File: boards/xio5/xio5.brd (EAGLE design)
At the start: 170 x 170 mm, 79 parts

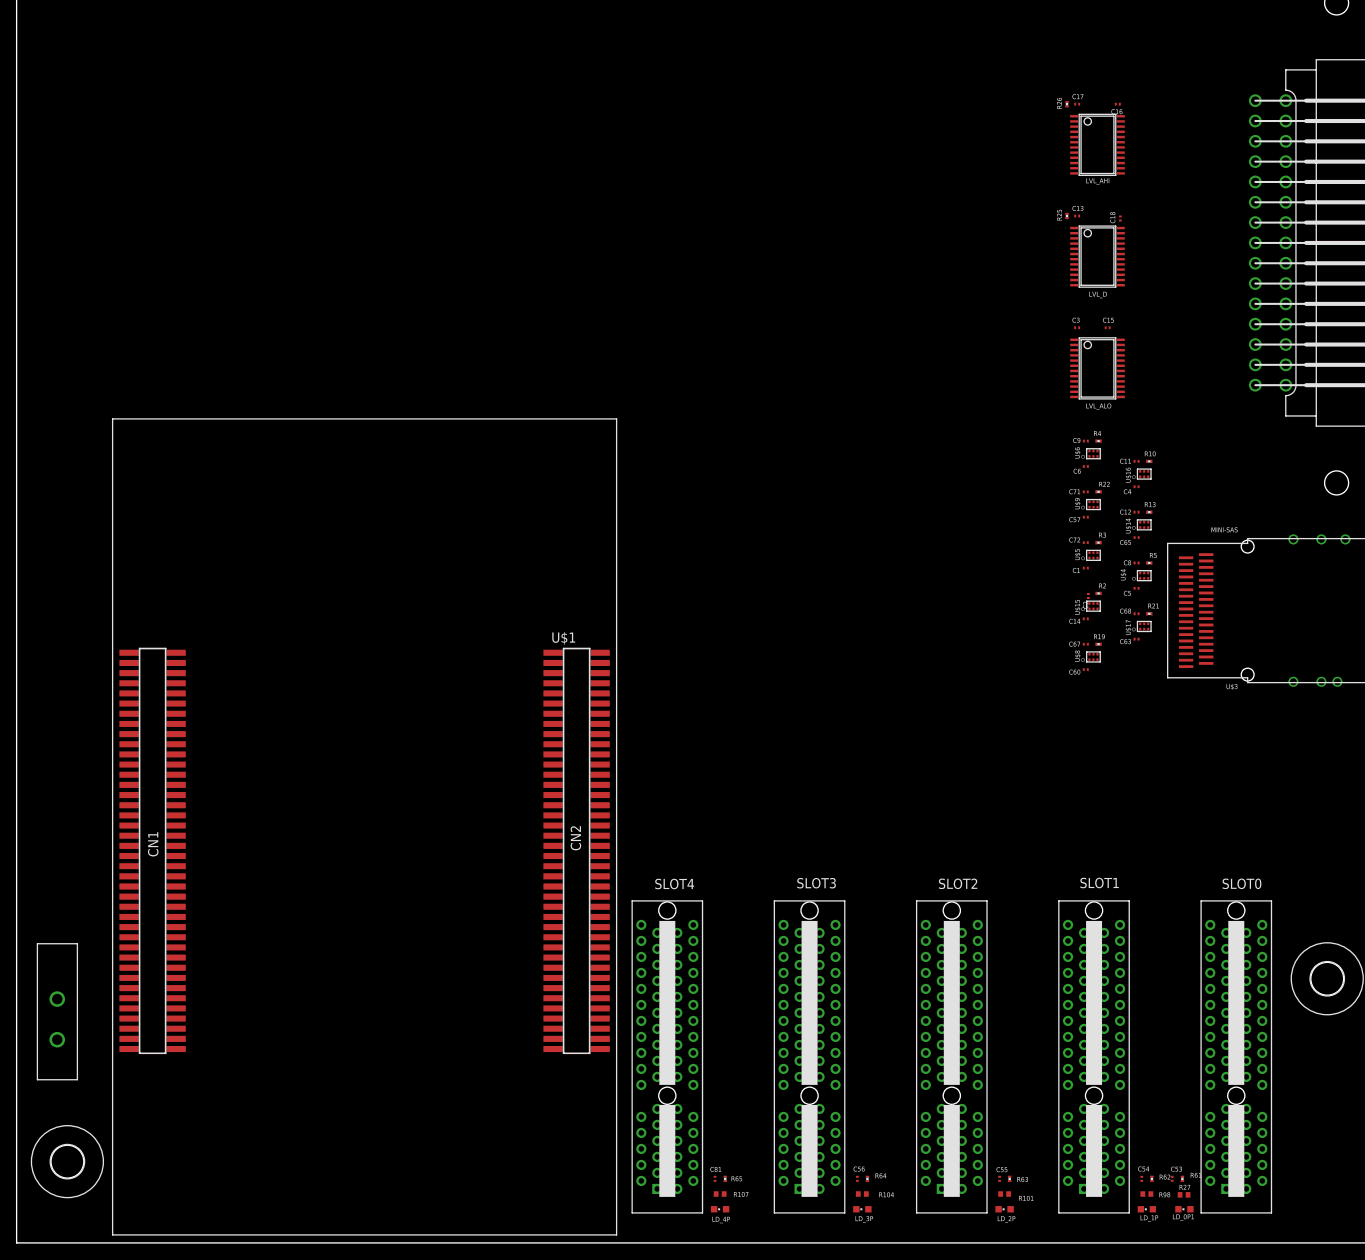
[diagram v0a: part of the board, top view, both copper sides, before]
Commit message: Start adding busses
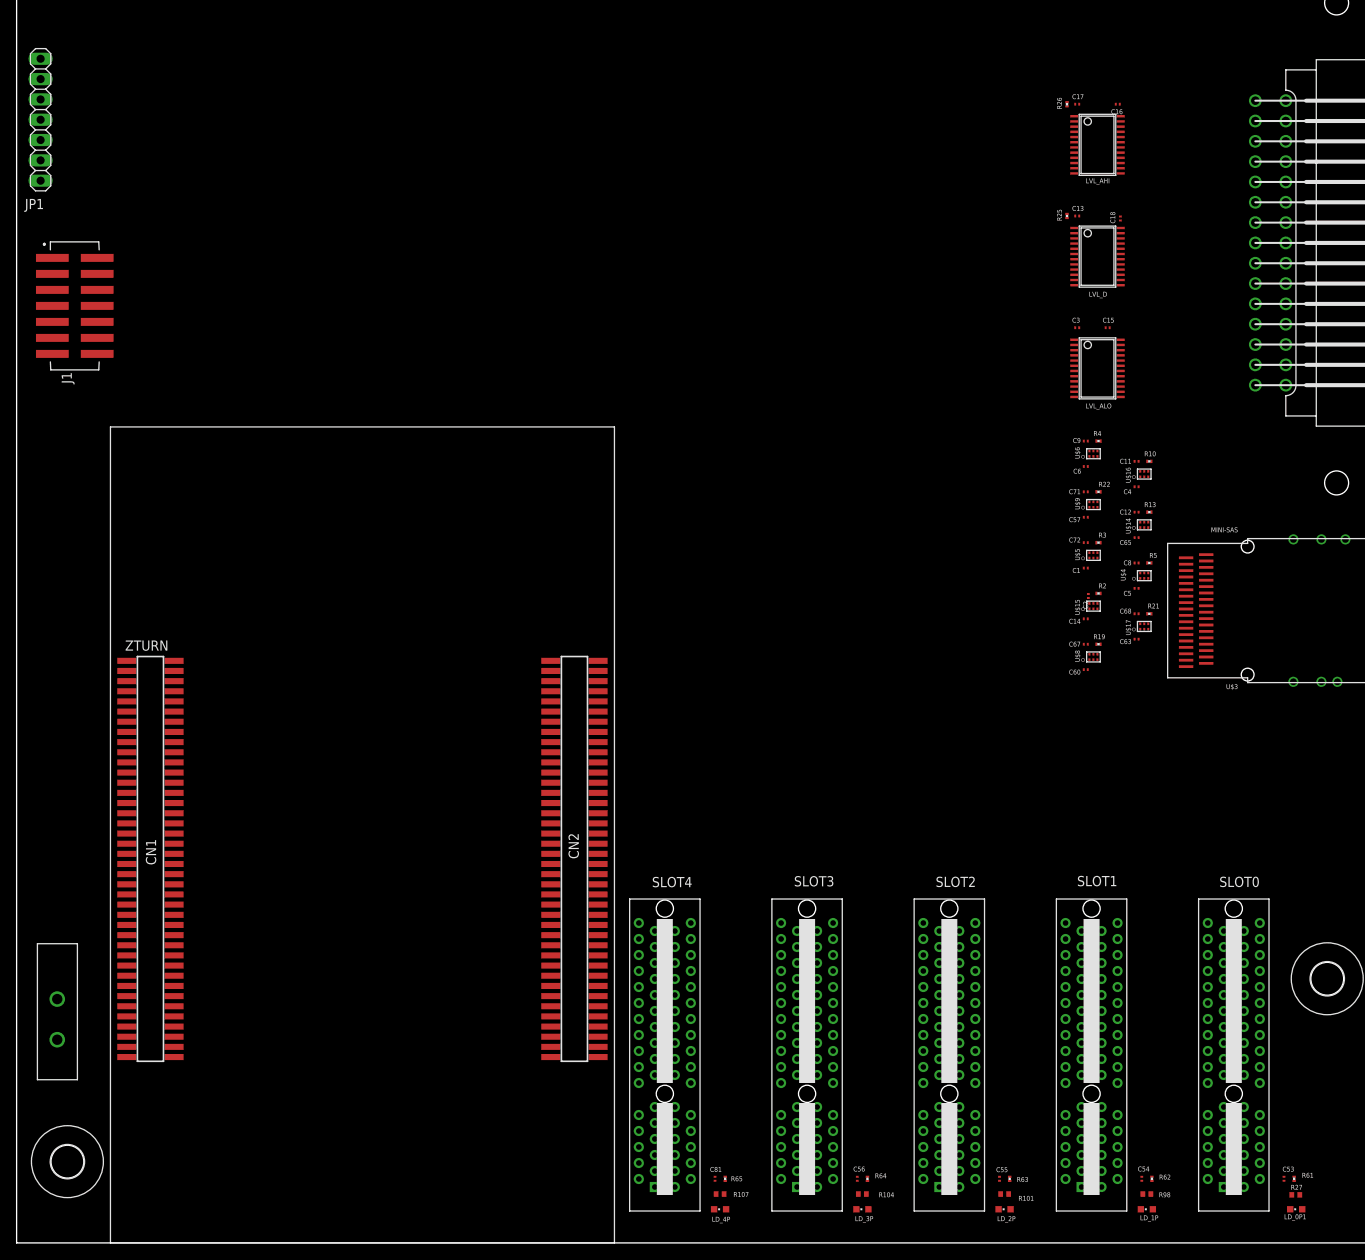
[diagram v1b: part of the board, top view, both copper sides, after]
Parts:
- removed U$1: ZTURN, pbxl:ZTURN
- added J1: 98424-G52-14ALF, samacsys:98424G5214ALF
- added JP1: (no value), pinhead:1X07
- added ZTURN: ZTURN, pbxl:ZTURN
- moved C53 14.0 mm to (158.4, 8.02)
- moved LD_0P1 14.0 mm to (159.9, 4.21)
- moved R27 14.0 mm to (159.9, 6.01)
- moved R61 14.0 mm to (159.7, 8.02)
- moved SLOT0 0.39 mm to (152.4, 19.1)
- moved SLOT1 0.39 mm to (134.6, 19.1)
- moved SLOT2 0.39 mm to (116.8, 19.1)
- moved SLOT3 0.39 mm to (99.1, 19.1)
- moved SLOT4 0.39 mm to (81.3, 19.1)
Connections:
- new net !SRST!: J1.B7, JP1.6, ZTURN.CN1_14
- new net TCK: J1.B3, JP1.3, ZTURN.CN1_6
- new net TDI: J1.B5, JP1.5, ZTURN.CN1_10
- new net TDO: J1.B4, JP1.4, ZTURN.CN1_12
- new net TMS: J1.B2, JP1.2, ZTURN.CN1_8
- net +3V3: now also J1.B1, JP1.1, ZTURN.CN1_15, ZTURN.CN1_3, ZTURN.CN1_49, ZTURN.CN2_3, ZTURN.CN2_51
- net +5V: now also ZTURN.CN1_1, ZTURN.CN2_1
- net GND: now also J1.A1, J1.A2, J1.A3, J1.A4, J1.A5, J1.A6, J1.A7, JP1.7, ZTURN.CN1_2, ZTURN.CN1_24, ZTURN.CN1_25, ZTURN.CN1_34, ZTURN.CN1_35, ZTURN.CN1_4, ZTURN.CN1_44, ZTURN.CN1_54, ZTURN.CN1_67, ZTURN.CN1_68, ZTURN.CN2_2, ZTURN.CN2_20, ZTURN.CN2_21, ZTURN.CN2_30, ZTURN.CN2_31, ZTURN.CN2_4, ZTURN.CN2_40, ZTURN.CN2_41, ZTURN.CN2_50, ZTURN.CN2_60, ZTURN.CN2_61, ZTURN.CN2_70, ZTURN.CN2_71, ZTURN.CN2_80
- net LO_A0: now also ZTURN.CN2_59
- net LO_A1: now also ZTURN.CN2_57
- net LO_A10: now also ZTURN.CN2_35
- net LO_A11: now also ZTURN.CN2_33
- net LO_A12: now also ZTURN.CN2_29
- net LO_A13: now also ZTURN.CN2_27
- net LO_A14: now also ZTURN.CN2_25
- net LO_A15: now also ZTURN.CN2_23
- net LO_A2: now also ZTURN.CN2_55
- net LO_A3: now also ZTURN.CN2_53
- net LO_A4: now also ZTURN.CN2_49
- net LO_A5: now also ZTURN.CN2_47
- net LO_A6: now also ZTURN.CN2_45
- net LO_A7: now also ZTURN.CN2_43
- net LO_A8: now also ZTURN.CN2_39
- net LO_A9: now also ZTURN.CN2_37
- net LO_D0: now also ZTURN.CN2_79
- net LO_D1: now also ZTURN.CN2_77
- net LO_D2: now also ZTURN.CN2_75
- net LO_D3: now also ZTURN.CN2_73
- net LO_D4: now also ZTURN.CN2_69
- net LO_D5: now also ZTURN.CN2_67
- net LO_D6: now also ZTURN.CN2_65
- net LO_D7: now also ZTURN.CN2_63

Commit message: Reorganise slot signals (ZBUS) and add the internal slot expansion interface (XBUS)
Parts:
- moved LD_4P 72.4 mm to (160.3, 5.47)
- moved R107 72.4 mm to (160.3, 7.38)
- moved R65 72.4 mm to (161.0, 9.29)
- moved C81 72.4 mm to (159.7, 9.29)
- moved SLOT4 72.4 mm to (153.7, 20.3)
- moved C53 69.9 mm to (88.6, 9.29)
- moved LD_0P1 69.9 mm to (90.1, 5.47)
- moved R27 69.9 mm to (90.0, 7.28)
- moved SLOT0 69.9 mm to (82.5, 20.3)
- moved R61 69.9 mm to (89.8, 9.29)
- moved LD_3P 36.9 mm to (142.6, 5.47)
- moved R104 36.9 mm to (142.6, 7.38)
- moved C56 36.9 mm to (141.9, 9.29)
- moved R64 36.9 mm to (143.2, 9.29)
- moved SLOT3 36.9 mm to (135.9, 20.3)
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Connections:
- removed net !LO_CCTL!: SLOT0.A27, SLOT1.A27, SLOT2.A27, SLOT3.A27, SLOT4.A27
- removed net !LO_REF!: SLOT0.B15, SLOT1.B15, SLOT2.B15, SLOT3.B15, SLOT4.B15
- removed net HBUS0: SLOT0.B18, SLOT1.B18, SLOT2.B18, SLOT3.B18, SLOT4.B18
- removed net HBUS1: SLOT0.B19, SLOT1.B19, SLOT2.B19, SLOT3.B19, SLOT4.B19
- removed net HBUS10: SLOT0.B28, SLOT1.B28, SLOT2.B28, SLOT3.B28, SLOT4.B28
- removed net HBUS11: SLOT0.B29, SLOT1.B29, SLOT2.B29, SLOT3.B29, SLOT4.B29
- removed net HBUS12: SLOT0.B30, SLOT1.B30, SLOT2.B30, SLOT3.B30, SLOT4.B30
- removed net HBUS13: SLOT0.B31, SLOT1.B31, SLOT2.B31, SLOT3.B31, SLOT4.B31
- removed net HBUS2: SLOT0.B20, SLOT1.B20, SLOT2.B20, SLOT3.B20, SLOT4.B20
- removed net HBUS3: SLOT0.B21, SLOT1.B21, SLOT2.B21, SLOT3.B21, SLOT4.B21
- removed net HBUS4: SLOT0.B22, SLOT1.B22, SLOT2.B22, SLOT3.B22, SLOT4.B22
- removed net HBUS5: SLOT0.B23, SLOT1.B23, SLOT2.B23, SLOT3.B23, SLOT4.B23
- removed net HBUS6: SLOT0.B24, SLOT1.B24, SLOT2.B24, SLOT3.B24, SLOT4.B24
- removed net HBUS7: SLOT0.B25, SLOT1.B25, SLOT2.B25, SLOT3.B25, SLOT4.B25
- removed net HBUS8: SLOT0.B26, SLOT1.B26, SLOT2.B26, SLOT3.B26, SLOT4.B26
- removed net HBUS9: SLOT0.B27, SLOT1.B27, SLOT2.B27, SLOT3.B27, SLOT4.B27
- removed net SPI0_IRQ: SLOT0.A8
- removed net SPI0_MOSI: SLOT0.A9
- removed net SPI1_IRQ: SLOT1.A8
- removed net SPI1_MISO: SLOT1.A10
- removed net SPI1_MOSI: SLOT1.A9
- removed net SPI2_IRQ: SLOT2.A8
- removed net SPI2_MISO: SLOT2.A10
- removed net SPI2_MOSI: SLOT2.A9
- removed net SPI3_IRQ: SLOT3.A8
- removed net SPI3_MISO: SLOT3.A10
- removed net SPI3_MOSI: SLOT3.A9
- removed net SPI4_IRQ: SLOT4.A8
- removed net SPI4_MISO: SLOT4.A10
- removed net SPI4_MOSI: SLOT4.A9
- removed net SPIO_MISO: SLOT0.A10
- removed net VALID_RD: SLOT0.A7, SLOT1.A7, SLOT2.A7, SLOT3.A7, SLOT4.A7
- removed net VALID_WR: SLOT0.A6, SLOT1.A6, SLOT2.A6, SLOT3.A6, SLOT4.A6
- new net !AVALID!: SLOT0.A9, SLOT1.A9, SLOT2.A9, SLOT3.A9, SLOT4.A9
- new net HSPI0_IRQ0: SLOT0.A7, ZTURN.CN2_74
- new net HSPI0_IRQ1: SLOT1.A7, ZTURN.CN2_72
- new net HSPI0_IRQ2: SLOT2.A7, ZTURN.CN2_68
- new net HSPI0_MISO: SLOT0.A4, SLOT1.A4, SLOT2.A4, ZTURN.CN2_78
- new net HSPI0_MOSI: SLOT0.A5, SLOT1.A5, SLOT2.A5, ZTURN.CN2_76
- new net HSPI0_SS0: SLOT0.A6, ZTURN.CN2_66
- new net HSPI0_SS1: SLOT1.A6, ZTURN.CN2_64
- new net HSPI0_SS2: SLOT2.A6, ZTURN.CN2_62
- new net HSPI1_IRQ0: SLOT3.A7, ZTURN.CN2_54
- new net HSPI1_IRQ1: SLOT4.A7, ZTURN.CN2_52
- new net HSPI1_IRQ2: ZTURN.CN2_48
- new net HSPI1_MISO: SLOT3.A4, SLOT4.A4, ZTURN.CN2_58
- new net HSPI1_MOSI: SLOT3.A5, SLOT4.A5, ZTURN.CN2_56
- new net HSPI1_SS0: SLOT3.A6, ZTURN.CN2_46
- new net HSPI1_SS1: SLOT4.A6, ZTURN.CN2_44
- new net HSPI1_SS2: ZTURN.CN2_42
- new net SX_PRESENT: ZTURN.CN2_26
- new net XBUS0: ZTURN.CN1_45
- new net XBUS1: ZTURN.CN1_47
- new net XBUS10: ZTURN.CN1_36
- new net XBUS11: ZTURN.CN1_38
- new net XBUS12: ZTURN.CN1_40
- new net XBUS13: ZTURN.CN1_42
- new net XBUS14: ZTURN.CN2_22
- new net XBUS15: ZTURN.CN2_24
- new net XBUS2: ZTURN.CN1_16
- new net XBUS3: ZTURN.CN1_18
- new net XBUS4: ZTURN.CN1_20
- new net XBUS5: ZTURN.CN1_22
- new net XBUS6: ZTURN.CN1_26
- new net XBUS7: ZTURN.CN1_28
- new net XBUS8: ZTURN.CN1_30
- new net XBUS9: ZTURN.CN1_32
- new net ZBUS0: SLOT0.B16, SLOT1.B16, SLOT2.B16, SLOT3.B16, SLOT4.B16, ZTURN.CN1_43
- new net ZBUS1: SLOT0.B17, SLOT1.B17, SLOT2.B17, SLOT3.B17, SLOT4.B17, ZTURN.CN1_41
- new net ZBUS10: SLOT0.B26, SLOT1.B26, SLOT2.B26, SLOT3.B26, SLOT4.B26, ZTURN.CN1_19
- new net ZBUS11: SLOT0.B27, SLOT1.B27, SLOT2.B27, SLOT3.B27, SLOT4.B27, ZTURN.CN1_17
- new net ZBUS12: SLOT0.B28, SLOT1.B28, SLOT2.B28, SLOT3.B28, SLOT4.B28, ZTURN.CN1_13
- new net ZBUS13: SLOT0.B29, SLOT1.B29, SLOT2.B29, SLOT3.B29, SLOT4.B29, ZTURN.CN1_11
- new net ZBUS14: SLOT0.B30, SLOT1.B30, SLOT2.B30, SLOT3.B30, SLOT4.B30, ZTURN.CN1_9
- new net ZBUS15: SLOT0.B31, SLOT1.B31, SLOT2.B31, SLOT3.B31, SLOT4.B31, ZTURN.CN1_7
- new net ZBUS2: SLOT0.B18, SLOT1.B18, SLOT2.B18, SLOT3.B18, SLOT4.B18, ZTURN.CN1_39
- new net ZBUS3: SLOT0.B19, SLOT1.B19, SLOT2.B19, SLOT3.B19, SLOT4.B19, ZTURN.CN1_37
- new net ZBUS4: SLOT0.B20, SLOT1.B20, SLOT2.B20, SLOT3.B20, SLOT4.B20, ZTURN.CN1_33
- new net ZBUS5: SLOT0.B21, SLOT1.B21, SLOT2.B21, SLOT3.B21, SLOT4.B21, ZTURN.CN1_31
- new net ZBUS6: SLOT0.B22, SLOT1.B22, SLOT2.B22, SLOT3.B22, SLOT4.B22, ZTURN.CN1_29
- new net ZBUS7: SLOT0.B23, SLOT1.B23, SLOT2.B23, SLOT3.B23, SLOT4.B23, ZTURN.CN1_27
- new net ZBUS8: SLOT0.B24, SLOT1.B24, SLOT2.B24, SLOT3.B24, SLOT4.B24, ZTURN.CN1_23
- new net ZBUS9: SLOT0.B25, SLOT1.B25, SLOT2.B25, SLOT3.B25, SLOT4.B25, ZTURN.CN1_21
- net !LO_RST!: now also SLOT0.A27, SLOT1.A27, SLOT2.A27, SLOT3.A27, SLOT4.A27; no longer SLOT0.B16, SLOT1.B16, SLOT2.B16, SLOT3.B16, SLOT4.B16
- net GND: now also SLOT0.A10, SLOT0.A8, SLOT1.A10, SLOT1.A8, SLOT2.A10, SLOT2.A8, SLOT3.A10, SLOT3.A8, SLOT4.A10, SLOT4.A8; no longer SLOT0.A4, SLOT0.A5, SLOT1.A4, SLOT1.A5, SLOT2.A4, SLOT2.A5, SLOT3.A4, SLOT3.A5, SLOT4.A4, SLOT4.A5
- net LO_A10: now also ZTURN.CN2_27; no longer ZTURN.CN2_35
- net LO_A11: now also ZTURN.CN2_29; no longer ZTURN.CN2_33
- net LO_A12: now also ZTURN.CN2_33; no longer ZTURN.CN2_29
- net LO_A13: now also ZTURN.CN2_35; no longer ZTURN.CN2_27
- net LO_A14: now also ZTURN.CN2_37; no longer ZTURN.CN2_25
- net LO_A15: now also ZTURN.CN2_39; no longer ZTURN.CN2_23
- net LO_A8: now also ZTURN.CN2_23; no longer ZTURN.CN2_39
- net LO_A9: now also ZTURN.CN2_25; no longer ZTURN.CN2_37
- net LO_R/!W!: now also SLOT0.B15, SLOT1.B15, SLOT2.B15, SLOT3.B15, SLOT4.B15; no longer SLOT0.B17, SLOT1.B17, SLOT2.B17, SLOT3.B17, SLOT4.B17
- net S0_PRESENT: now also ZTURN.CN2_38
- net S1_PRESENT: now also ZTURN.CN2_36
- net S2_PRESENT: now also ZTURN.CN2_34
- net S3_PRESENT: now also ZTURN.CN2_32
- net S4_PRESENT: now also ZTURN.CN2_28

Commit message: Work on some of the internal expansion stuff
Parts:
- added C19: 0.1uF, rcl:C0201
- added IC1: PCAL6416APW,118, samacsys:SOP65P640X110-24N
- added JP2: (no value), pinhead:2X02
- added JP3: (no value), pinhead-2:2X16M
- added LD_M0, LD_M1: Orange, led:CHIPLED_0603
- added R1, R6: 59R, rcl:R0402
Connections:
- removed net XBUS0: ZTURN.CN1_45
- removed net XBUS1: ZTURN.CN1_47
- removed net XBUS10: ZTURN.CN1_36
- removed net XBUS11: ZTURN.CN1_38
- removed net XBUS12: ZTURN.CN1_40
- removed net XBUS13: ZTURN.CN1_42
- removed net XBUS14: ZTURN.CN2_22
- removed net XBUS15: ZTURN.CN2_24
- removed net XBUS2: ZTURN.CN1_16
- removed net XBUS3: ZTURN.CN1_18
- removed net XBUS4: ZTURN.CN1_20
- removed net XBUS5: ZTURN.CN1_22
- removed net XBUS6: ZTURN.CN1_26
- removed net XBUS7: ZTURN.CN1_28
- removed net XBUS8: ZTURN.CN1_30
- removed net XBUS9: ZTURN.CN1_32
- new net N$2: IC1.11, R6.2
- new net N$3: LD_M1.A, R6.1
- new net N$4: IC1.1, ZTURN.CN2_36
- new net N$5: IC1.3, ZTURN.CN2_38
- new net N$7: IC1.10, R1.2
- new net N$8: LD_M0.A, R1.1
- new net SCL: IC1.22, JP2.2, ZTURN.CN1_78
- new net SDA: IC1.23, JP2.4, ZTURN.CN1_76
- new net XIO0: IC1.13, JP3.13
- new net XIO1: IC1.14, JP3.15
- new net XIO2: IC1.15, JP3.17
- new net XIO3: IC1.16, JP3.19
- new net XIO4: IC1.17, JP3.21
- new net XIO5: IC1.18, JP3.23
- new net XIO6: IC1.19, JP3.25
- new net XIO7: IC1.20, JP3.27
- new net XSPI_IRQ: JP3.5, ZTURN.CN2_28
- new net XSPI_MISO: JP2.1, JP3.7, ZTURN.CN2_32
- new net XSPI_MOSI: JP2.3, JP3.9, ZTURN.CN2_34
- net !LO_EXTSEL!: now also ZTURN.CN1_32
- net !LO_HALT!: now also ZTURN.CN1_36
- net !LO_IRQ!: now also ZTURN.CN1_38
- net !LO_MPD!: now also ZTURN.CN1_40
- net !LO_RST!: now also ZTURN.CN2_24
- net +3V3: now also C19.1, IC1.2, IC1.24
- net +5V: now also JP3.1, JP3.3
- net DIR_A: now also ZTURN.CN1_45
- net DIR_CLK: no longer U$15.5
- net DIR_D: now also ZTURN.CN1_47
- net DIR_EXTSEL: now also ZTURN.CN1_16
- net DIR_HALT: now also ZTURN.CN1_18
- net DIR_IRQ: now also ZTURN.CN1_20
- net DIR_MPD: now also ZTURN.CN1_22
- net DIR_RD4: no longer U$16.5
- net DIR_RD5: no longer U$14.5
- net DIR_RST: now also ZTURN.CN1_26
- net DIR_RW: now also ZTURN.CN1_28
- net GND: now also C19.2, IC1.12, IC1.21, JP3.29, JP3.31, LD_M0.C, LD_M1.C, U$14.5, U$15.5, U$16.5
- net LO_CLK: now also ZTURN.CN1_30
- net LO_R/!W!: now also ZTURN.CN2_26
- net LO_RD4: now also ZTURN.CN1_42
- net LO_RD5: now also ZTURN.CN2_22
- net S0_PRESENT: now also IC1.4; no longer ZTURN.CN2_38
- net S1_PRESENT: now also IC1.5; no longer ZTURN.CN2_36
- net S2_PRESENT: now also IC1.6; no longer ZTURN.CN2_34
- net S3_PRESENT: now also IC1.7; no longer ZTURN.CN2_32
- net S4_PRESENT: now also IC1.8; no longer ZTURN.CN2_28
- net SX_PRESENT: now also IC1.9, JP3.11; no longer ZTURN.CN2_26
- net ZBUS0: now also JP3.32
- net ZBUS1: now also JP3.30
- net ZBUS10: now also JP3.12
- net ZBUS11: now also JP3.10
- net ZBUS12: now also JP3.8
- net ZBUS13: now also JP3.6
- net ZBUS14: now also JP3.4
- net ZBUS15: now also JP3.2
- net ZBUS2: now also JP3.28
- net ZBUS3: now also JP3.26
- net ZBUS4: now also JP3.24
- net ZBUS5: now also JP3.22
- net ZBUS6: now also JP3.20
- net ZBUS7: now also JP3.18
- net ZBUS8: now also JP3.16
- net ZBUS9: now also JP3.14
